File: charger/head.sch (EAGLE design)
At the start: 5 parts

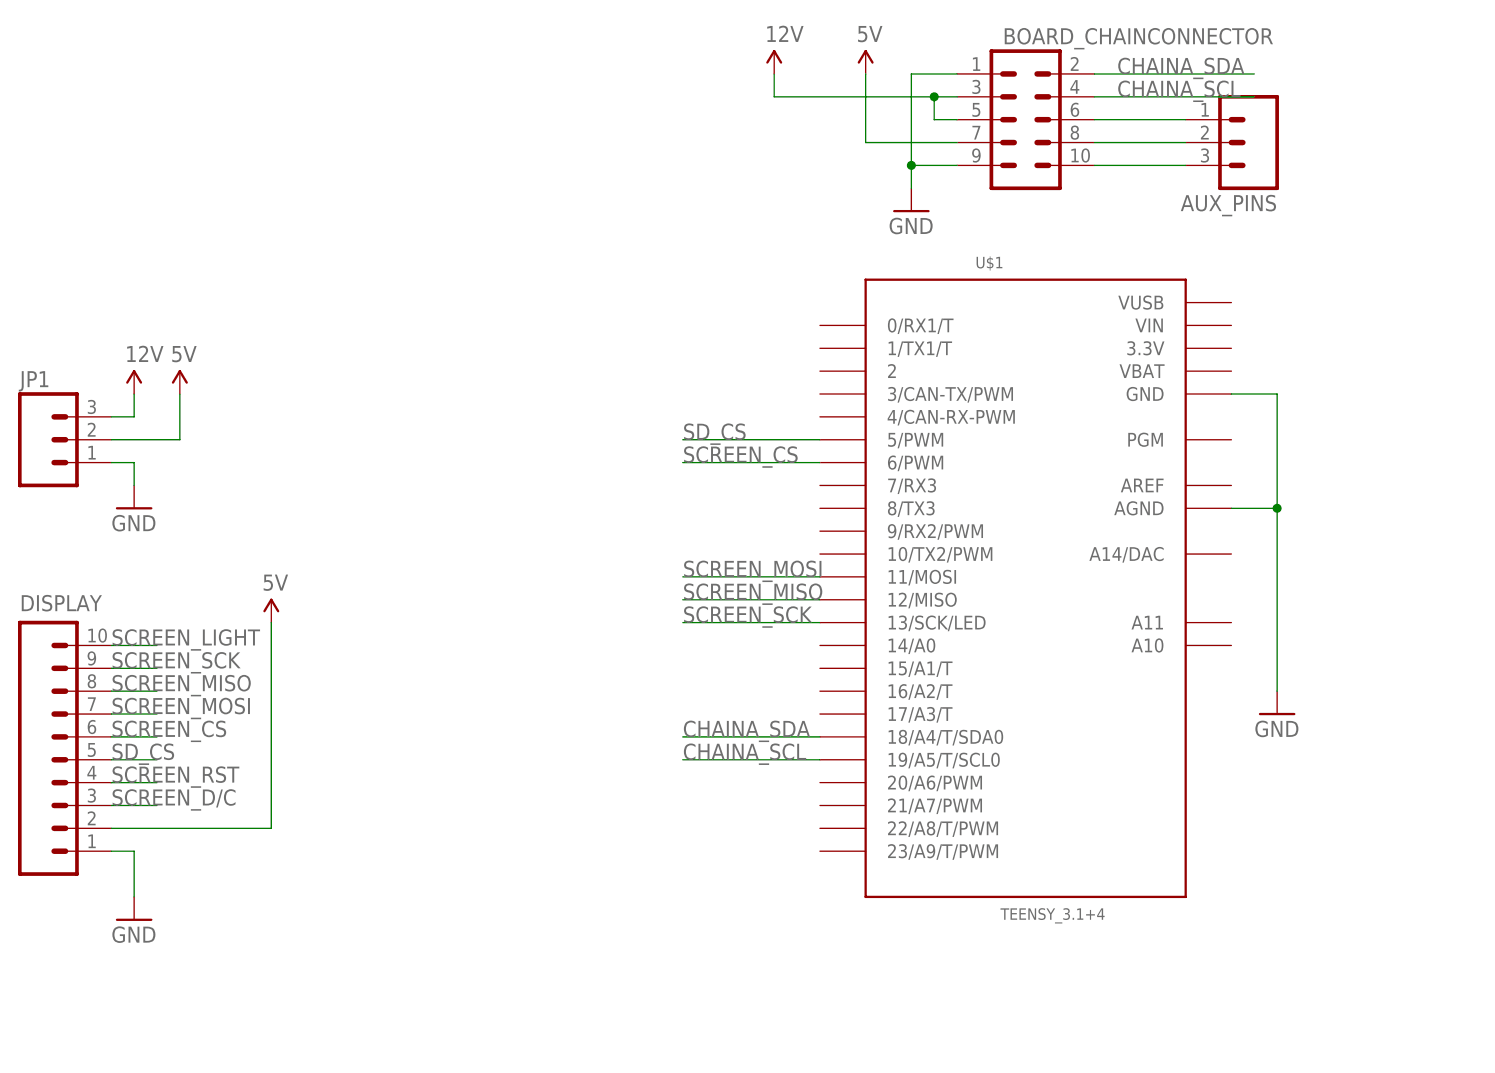
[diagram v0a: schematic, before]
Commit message: Improve the design and layout of the charger head
- smaller board
- wire up Teensy to power
- add ws2812 status led
- add filtering caps
- add mounting holes
- downgrade to 3x2 header for interboard comms
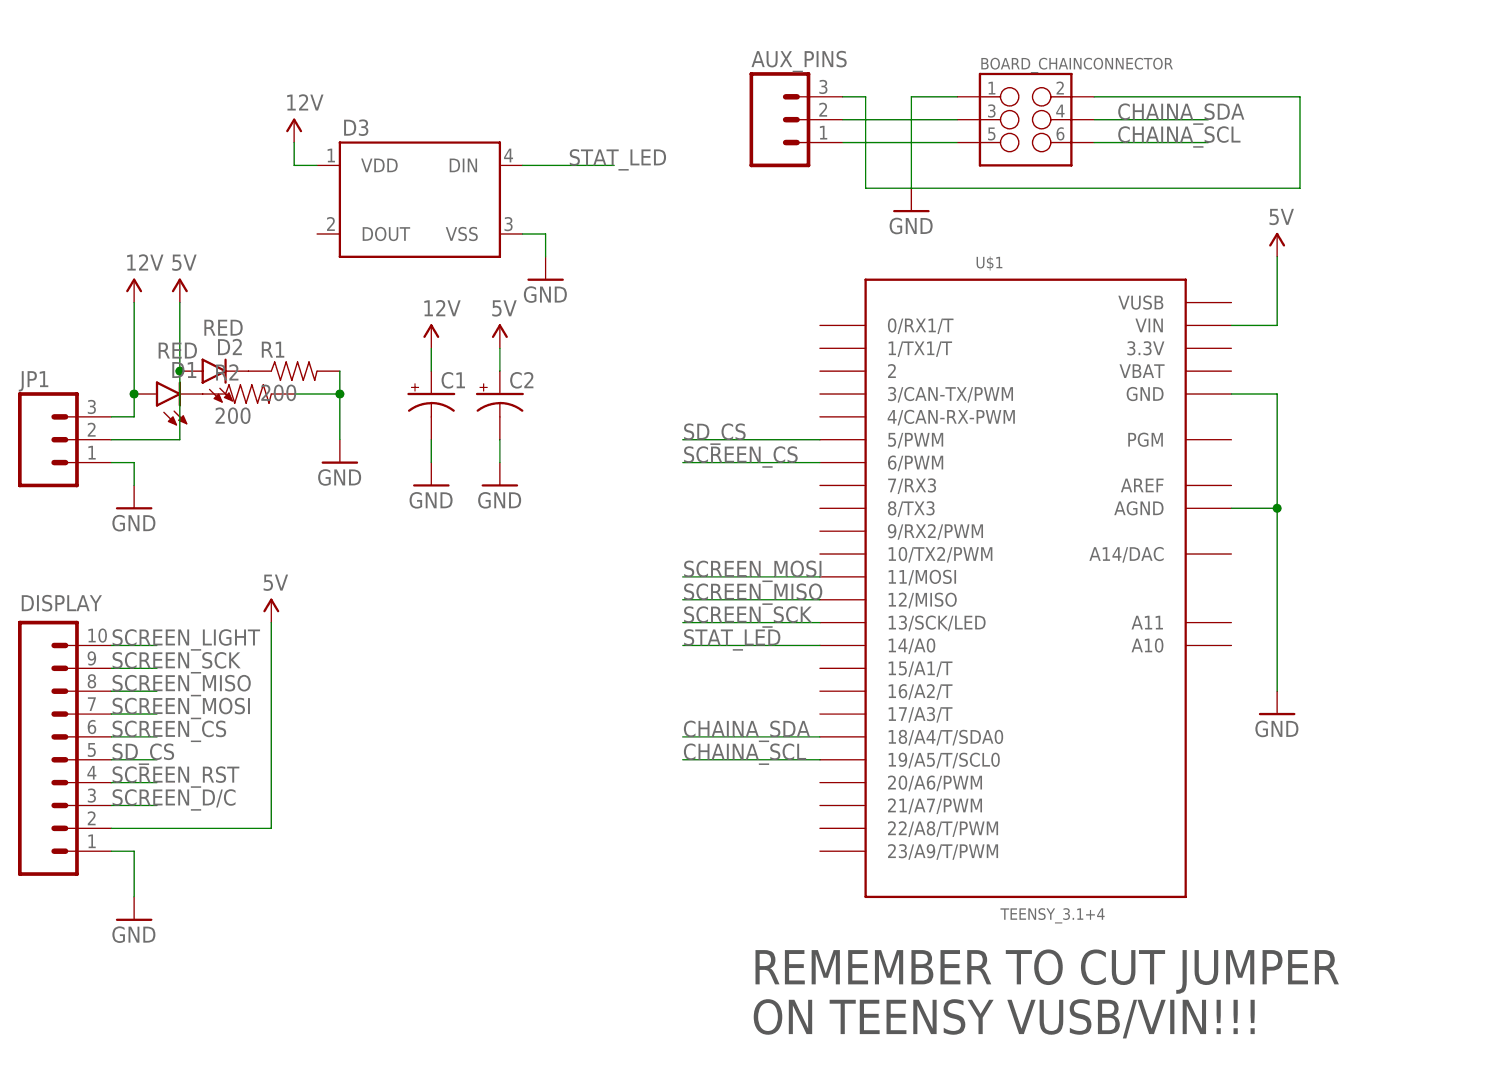
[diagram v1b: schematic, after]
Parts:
- added C1, C2: (no value), SparkFun-Capacitors:100UF-25V-20%(PTH)
- added D1, D2: RED, SparkFun-LED:LED-RED1206
- added D3: (no value), SparkFun-LED:WS2812B
- added R1, R2: 200, SparkFun-Resistors:200OHM1/10W1%(0603)
- BOARD_CHAINCONNECTOR: device SparkFun-Connectors:M05X2SHD -> SparkFun-Connectors:M03X22X3_SILK_MALE_PTH
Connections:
- new net N$4: D2.C, R1.1
- new net N$5: D1.C, R2.1
- new net STAT_LED: D3.DIN, U$1.14/A0
- net 12V: now also C1.+, D1.A, D3.VDD; no longer BOARD_CHAINCONNECTOR.3, BOARD_CHAINCONNECTOR.5
- net 5V: now also C2.+, D2.A, U$1.VIN; no longer BOARD_CHAINCONNECTOR.7
- net CHAINA_SCL: now also BOARD_CHAINCONNECTOR.6; no longer BOARD_CHAINCONNECTOR.4
- net CHAINA_SDA: now also BOARD_CHAINCONNECTOR.4; no longer BOARD_CHAINCONNECTOR.2
- net GND: now also C1.-, C2.-, D3.VSS, R1.2, R2.2; no longer BOARD_CHAINCONNECTOR.9
- net N$1: now also BOARD_CHAINCONNECTOR.3; no longer BOARD_CHAINCONNECTOR.8
- net N$2: now also AUX_PINS.1, BOARD_CHAINCONNECTOR.5; no longer AUX_PINS.3, BOARD_CHAINCONNECTOR.10
- net N$3: now also AUX_PINS.3, BOARD_CHAINCONNECTOR.2; no longer AUX_PINS.1, BOARD_CHAINCONNECTOR.6
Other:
- note added: "REMEMBER TO CUT JUMPER ON TEENSY VUSB/VIN!!!"
- moved on the sheet: AUX_PINS

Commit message: Add a few nice things to the control head
- break out a bunch of teensy pins
- add a resistor to the ws2812 for reliability
- a bit of rerouting
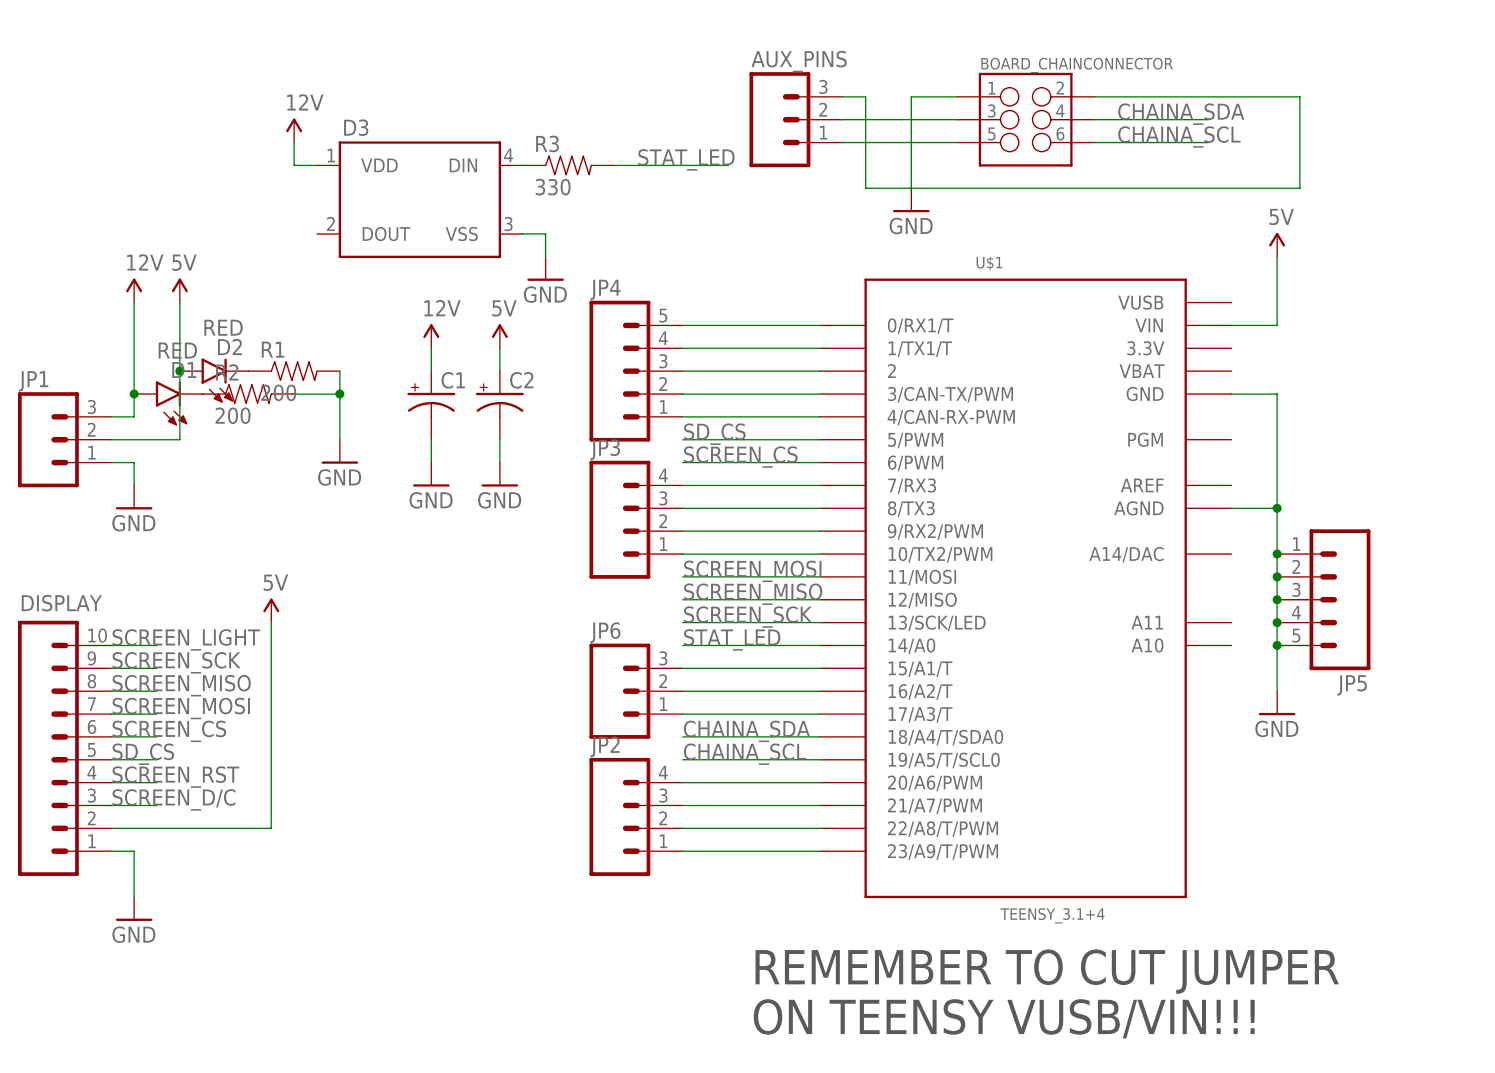
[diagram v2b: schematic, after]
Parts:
- added JP2, JP3: (no value), SparkFun-Connectors:M04PTH
- added JP4, JP5: (no value), SparkFun-Connectors:M05PTH
- added JP6: (no value), SparkFun-Connectors:M03PTH
- added R3: 330, SparkFun-Resistors:RESISTORPTH-1/4W-VERT-KIT
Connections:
- new net N$10: JP2.2, U$1.22/A8/T/PWM
- new net N$11: JP2.1, U$1.23/A9/T/PWM
- new net N$12: JP3.1, U$1.10/TX2/PWM
- new net N$13: JP3.2, U$1.9/RX2/PWM
- new net N$14: JP3.3, U$1.8/TX3
- new net N$15: JP3.4, U$1.7/RX3
- new net N$16: JP4.1, U$1.4/CAN-RX-PWM
- new net N$17: JP4.2, U$1.3/CAN-TX/PWM
- new net N$18: JP4.3, U$1.2
- new net N$19: JP4.4, U$1.1/TX1/T
- new net N$20: JP4.5, U$1.0/RX1/T
- new net N$21: JP6.2, U$1.16/A2/T
- new net N$22: JP6.1, U$1.17/A3/T
- new net N$6: D3.DIN, R3.1
- new net N$7: JP6.3, U$1.15/A1/T
- new net N$8: JP2.4, U$1.20/A6/PWM
- new net N$9: JP2.3, U$1.21/A7/PWM
- net GND: now also JP5.1, JP5.2, JP5.3, JP5.4, JP5.5
- net STAT_LED: now also R3.2; no longer D3.DIN
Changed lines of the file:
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@@
 <part name="GND7" library="SparkFun-Aesthetics" deviceset="GND" device=""/>
 <part name="GND8" library="SparkFun-Aesthetics" deviceset="GND" device=""/>
+<part name="JP2" library="SparkFun-Connectors" deviceset="M04" device="PTH"/>
+<part name="JP3" library="SparkFun-Connectors" deviceset="M04" device="PTH"/>
+<part name="JP4" library="SparkFun-Connectors" deviceset="M05" device="PTH"/>
+<part name="JP5" library="SparkFun-Connectors" deviceset="M05" device="PTH"/>
+<part name="R3" library="SparkFun-Resistors" deviceset="RESISTOR" device="PTH-1/4W-VERT-KIT" value="330"/>
+<part name="JP6" library="SparkFun-Connectors" deviceset="M03" device="PTH"/>
 </parts>
 <sheets>
@@
 <instance part="GND7" gate="1" x="73.66" y="55.88"/>
 <instance part="GND8" gate="1" x="81.28" y="55.88"/>
+<instance part="JP2" gate="G$1" x="96.52" y="17.78"/>
+<instance part="JP3" gate="G$1" x="96.52" y="50.8"/>
+<instance part="JP4" gate="G$1" x="93.98" y="68.58"/>
+<instance part="JP5" gate="G$1" x="175.26" y="43.18" rot="R180"/>
+<instance part="R3" gate="G$1" x="88.9" y="91.44"/>
+<instance part="JP6" gate="G$1" x="93.98" y="33.02"/>
 </instances>
 <busses>
@@
 <wire x1="167.64" y1="66.04" x2="167.64" y2="53.34" width="0.1524" layer="91"/>
 <pinref part="U$1" gate="G$1" pin="AGND"/>
-<wire x1="167.64" y1="53.34" x2="167.64" y2="33.02" width="0.1524" layer="91"/>
+<wire x1="167.64" y1="53.34" x2="167.64" y2="48.26" width="0.1524" layer="91"/>
+<wire x1="167.64" y1="48.26" x2="167.64" y2="45.72" width="0.1524" layer="91"/>
+<wire x1="167.64" y1="45.72" x2="167.64" y2="43.18" width="0.1524" layer="91"/>
+<wire x1="167.64" y1="43.18" x2="167.64" y2="40.64" width="0.1524" layer="91"/>
+<wire x1="167.64" y1="40.64" x2="167.64" y2="38.1" width="0.1524" layer="91"/>
+<wire x1="167.64" y1="38.1" x2="167.64" y2="33.02" width="0.1524" layer="91"/>
 <wire x1="162.56" y1="53.34" x2="167.64" y2="53.34" width="0.1524" layer="91"/>
 <junction x="167.64" y="53.34"/>
+<pinref part="JP5" gate="G$1" pin="1"/>
+<junction x="167.64" y="48.26"/>
+<pinref part="JP5" gate="G$1" pin="2"/>
+<junction x="167.64" y="45.72"/>
+<pinref part="JP5" gate="G$1" pin="3"/>
+<junction x="167.64" y="43.18"/>
+<pinref part="JP5" gate="G$1" pin="4"/>
+<junction x="167.64" y="40.64"/>
+<pinref part="JP5" gate="G$1" pin="5"/>
+<junction x="167.64" y="38.1"/>
 </segment>
 <segment>
@@
 <net name="STAT_LED" class="0">
 <segment>
-<pinref part="D3" gate="G$1" pin="DIN"/>
-<wire x1="83.82" y1="91.44" x2="93.98" y2="91.44" width="0.1524" layer="91"/>
-<label x="88.9" y="91.44" size="1.778" layer="95"/>
-</segment>
-<segment>
 <pinref part="U$1" gate="G$1" pin="14/A0"/>
 <wire x1="101.6" y1="38.1" x2="116.84" y2="38.1" width="0.1524" layer="91"/>
 <label x="101.6" y="38.1" size="1.778" layer="95"/>
+</segment>
+<segment>
+<pinref part="R3" gate="G$1" pin="2"/>
+<wire x1="93.98" y1="91.44" x2="106.68" y2="91.44" width="0.1524" layer="91"/>
+<label x="96.52" y="91.44" size="1.778" layer="95"/>
 </segment>
 </net>
@@
 </segment>
 </net>
+<net name="N$8" class="0">
+<segment>
+<pinref part="JP2" gate="G$1" pin="4"/>
+<pinref part="U$1" gate="G$1" pin="20/A6/PWM"/>
+<wire x1="101.6" y1="22.86" x2="116.84" y2="22.86" width="0.1524" layer="91"/>
+</segment>
+</net>
+<net name="N$9" class="0">
+<segment>
+<pinref part="JP2" gate="G$1" pin="3"/>
+<pinref part="U$1" gate="G$1" pin="21/A7/PWM"/>
+<wire x1="101.6" y1="20.32" x2="116.84" y2="20.32" width="0.1524" layer="91"/>
+</segment>
+</net>
+<net name="N$10" class="0">
+<segment>
+<pinref part="JP2" gate="G$1" pin="2"/>
+<pinref part="U$1" gate="G$1" pin="22/A8/T/PWM"/>
+<wire x1="101.6" y1="17.78" x2="116.84" y2="17.78" width="0.1524" layer="91"/>
+</segment>
+</net>
+<net name="N$11" class="0">
+<segment>
+<pinref part="JP2" gate="G$1" pin="1"/>
+<pinref part="U$1" gate="G$1" pin="23/A9/T/PWM"/>
+<wire x1="101.6" y1="15.24" x2="116.84" y2="15.24" width="0.1524" layer="91"/>
+</segment>
+</net>
+<net name="N$12" class="0">
+<segment>
+<pinref part="JP3" gate="G$1" pin="1"/>
+<pinref part="U$1" gate="G$1" pin="10/TX2/PWM"/>
+<wire x1="101.6" y1="48.26" x2="116.84" y2="48.26" width="0.1524" layer="91"/>
+</segment>
+</net>
+<net name="N$13" class="0">
+<segment>
+<pinref part="U$1" gate="G$1" pin="9/RX2/PWM"/>
+<pinref part="JP3" gate="G$1" pin="2"/>
+<wire x1="116.84" y1="50.8" x2="101.6" y2="50.8" width="0.1524" layer="91"/>
+</segment>
+</net>
+<net name="N$14" class="0">
+<segment>
+<pinref part="JP3" gate="G$1" pin="3"/>
+<pinref part="U$1" gate="G$1" pin="8/TX3"/>
+<wire x1="101.6" y1="53.34" x2="116.84" y2="53.34" width="0.1524" layer="91"/>
+</segment>
+</net>
+<net name="N$15" class="0">
+<segment>
+<pinref part="U$1" gate="G$1" pin="7/RX3"/>
+<pinref part="JP3" gate="G$1" pin="4"/>
+<wire x1="116.84" y1="55.88" x2="101.6" y2="55.88" width="0.1524" layer="91"/>
+</segment>
+</net>
+<net name="N$16" class="0">
+<segment>
+<pinref part="JP4" gate="G$1" pin="1"/>
+<pinref part="U$1" gate="G$1" pin="4/CAN-RX-PWM"/>
+<wire x1="101.6" y1="63.5" x2="116.84" y2="63.5" width="0.1524" layer="91"/>
+</segment>
+</net>
+<net name="N$17" class="0">
+<segment>
+<pinref part="U$1" gate="G$1" pin="3/CAN-TX/PWM"/>
+<pinref part="JP4" gate="G$1" pin="2"/>
+<wire x1="116.84" y1="66.04" x2="101.6" y2="66.04" width="0.1524" layer="91"/>
+</segment>
+</net>
+<net name="N$18" class="0">
+<segment>
+<pinref part="JP4" gate="G$1" pin="3"/>
+<pinref part="U$1" gate="G$1" pin="2"/>
+<wire x1="101.6" y1="68.58" x2="116.84" y2="68.58" width="0.1524" layer="91"/>
+</segment>
+</net>
+<net name="N$19" class="0">
+<segment>
+<pinref part="U$1" gate="G$1" pin="1/TX1/T"/>
+<pinref part="JP4" gate="G$1" pin="4"/>
+<wire x1="116.84" y1="71.12" x2="101.6" y2="71.12" width="0.1524" layer="91"/>
+</segment>
+</net>
+<net name="N$20" class="0">
+<segment>
+<pinref part="JP4" gate="G$1" pin="5"/>
+<wire x1="101.6" y1="73.66" x2="116.84" y2="73.66" width="0.1524" layer="91"/>
+<pinref part="U$1" gate="G$1" pin="0/RX1/T"/>
+</segment>
+</net>
+<net name="N$6" class="0">
+<segment>
+<pinref part="D3" gate="G$1" pin="DIN"/>
+<pinref part="R3" gate="G$1" pin="1"/>
+</segment>
+</net>
+<net name="N$7" class="0">
+<segment>
+<pinref part="JP6" gate="G$1" pin="3"/>
+<pinref part="U$1" gate="G$1" pin="15/A1/T"/>
+<wire x1="101.6" y1="35.56" x2="116.84" y2="35.56" width="0.1524" layer="91"/>
+</segment>
+</net>
+<net name="N$21" class="0">
+<segment>
+<pinref part="JP6" gate="G$1" pin="2"/>
+<pinref part="U$1" gate="G$1" pin="16/A2/T"/>
+<wire x1="101.6" y1="33.02" x2="116.84" y2="33.02" width="0.1524" layer="91"/>
+</segment>
+</net>
+<net name="N$22" class="0">
+<segment>
+<pinref part="JP6" gate="G$1" pin="1"/>
+<pinref part="U$1" gate="G$1" pin="17/A3/T"/>
+<wire x1="101.6" y1="30.48" x2="116.84" y2="30.48" width="0.1524" layer="91"/>
+</segment>
+</net>
